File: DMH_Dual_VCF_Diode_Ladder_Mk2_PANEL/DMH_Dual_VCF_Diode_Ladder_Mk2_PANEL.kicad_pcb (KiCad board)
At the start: 2 copper layers, 150 x 200 mm, 55 parts, among them J0 Panel_GND_Solder_Wire_Pad

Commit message: KiCad 9.0.7 + centralized library
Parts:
- H40, H42: footprint SynthStuff:MountingHole_LED_3mm -> SynthStuff:MountingHole_LED_3mm_R
- H41: footprint SynthStuff:MountingHole_LED_3mm -> SynthStuff:MountingHole_LED_3mm_B

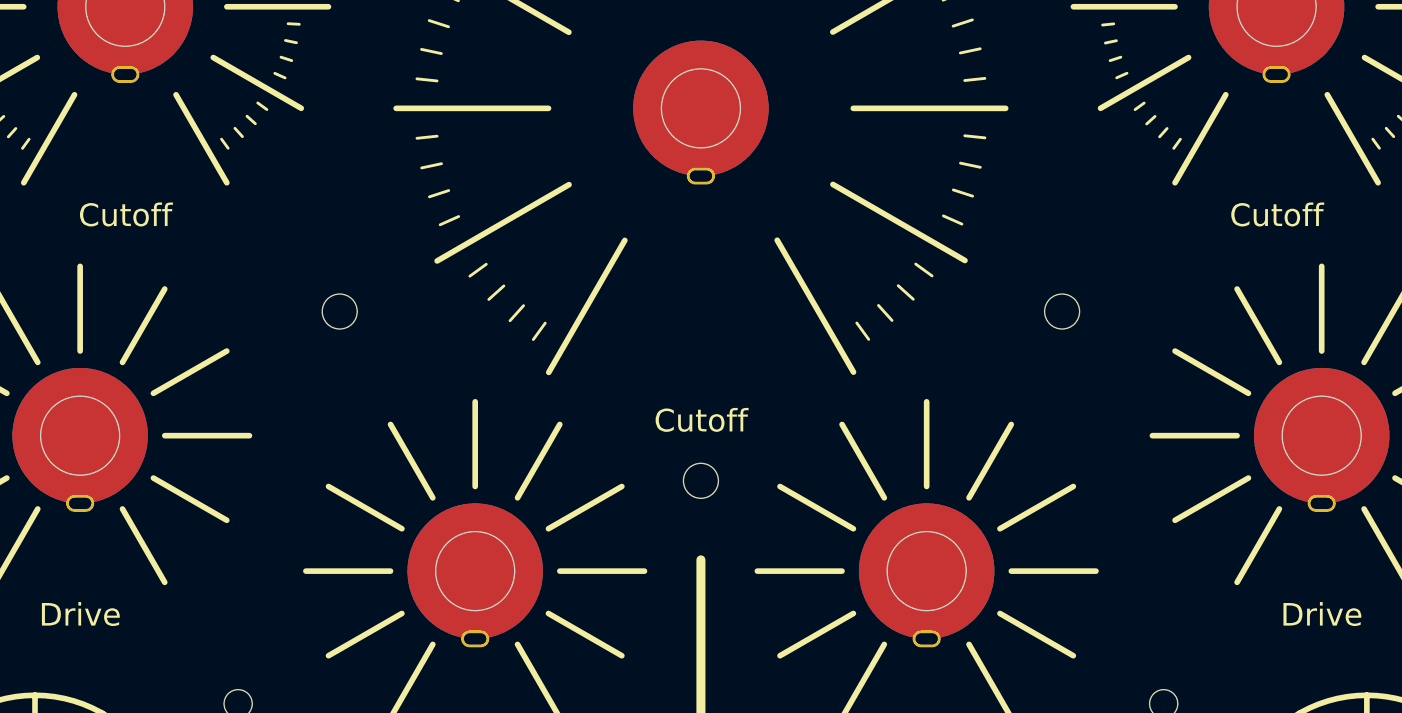
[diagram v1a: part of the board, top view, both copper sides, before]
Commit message: KiCad 10
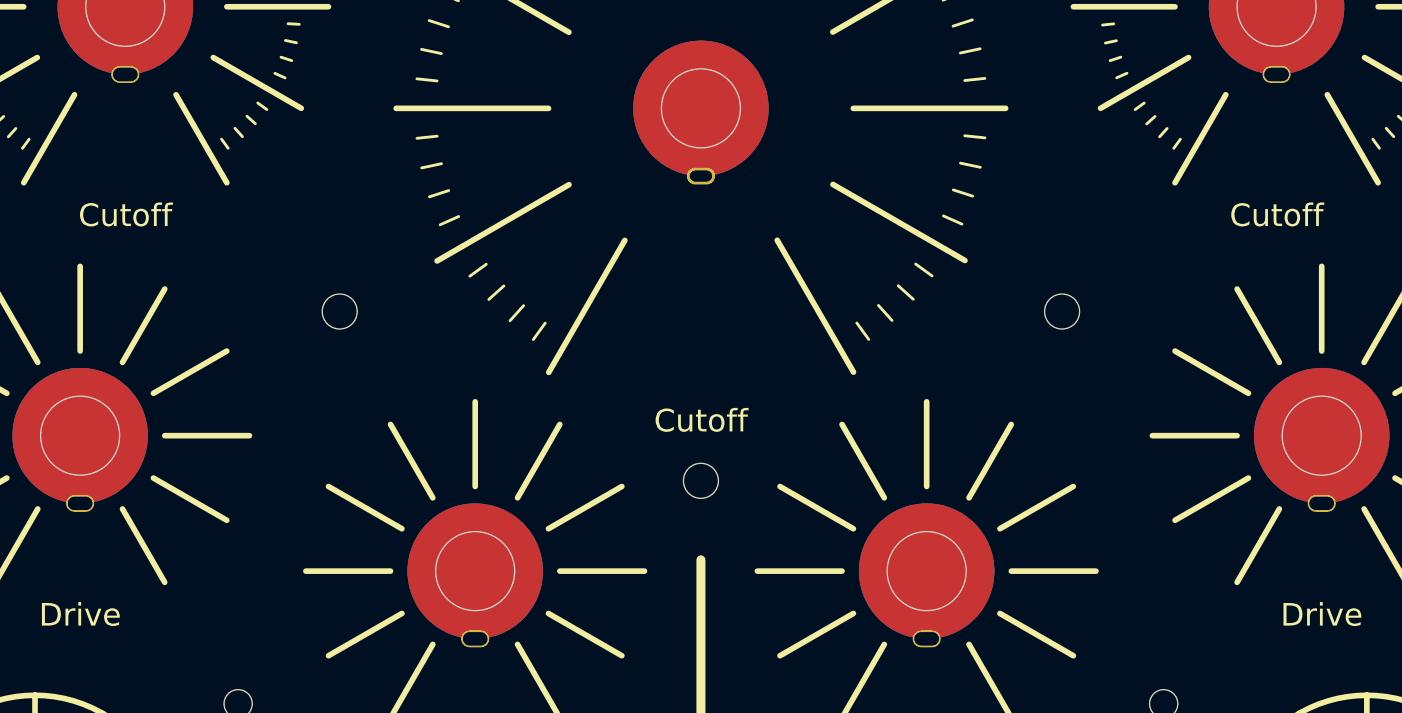
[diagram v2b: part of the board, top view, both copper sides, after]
